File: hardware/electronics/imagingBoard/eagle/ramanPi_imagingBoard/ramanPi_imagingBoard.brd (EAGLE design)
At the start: 107.9 x 79.7 mm, 14 parts

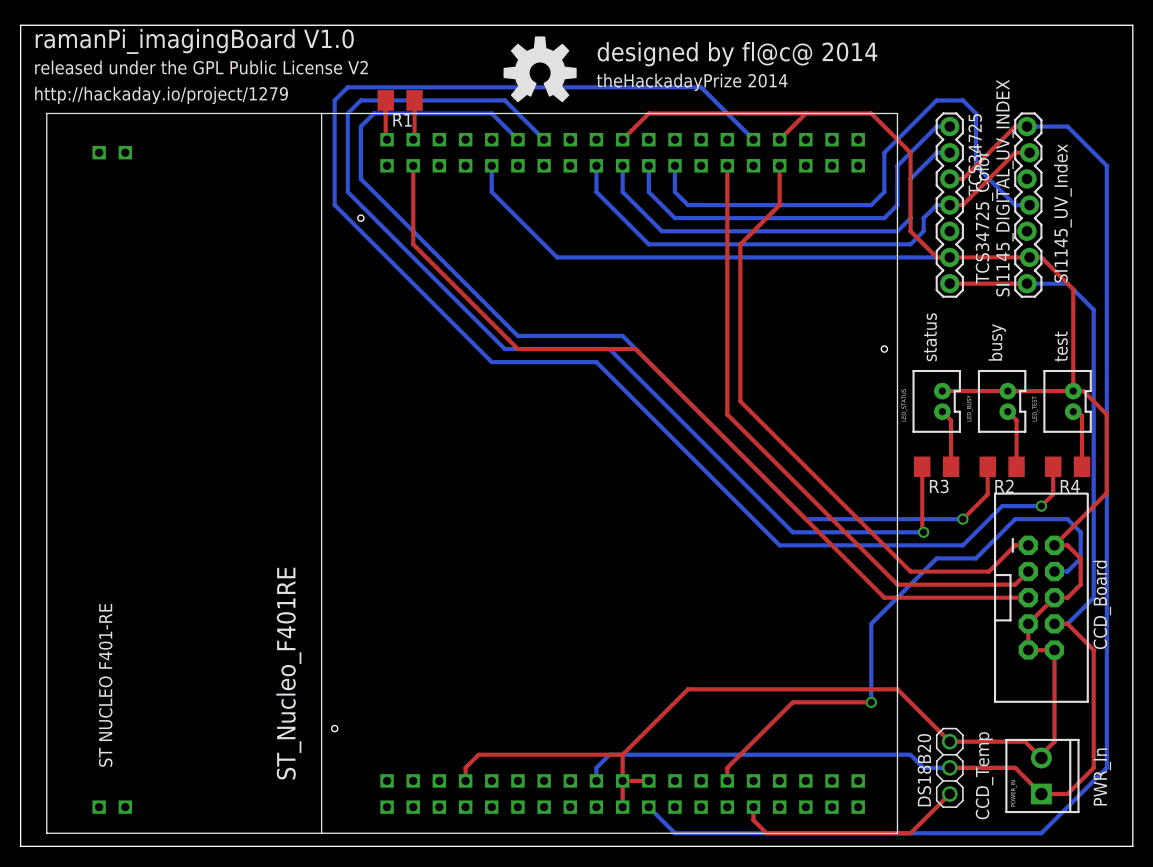
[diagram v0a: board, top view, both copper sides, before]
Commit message: imagingBoard updated
updated pin configuration for remote ccd board to match with new pinout
added ground plane and decoupling caps
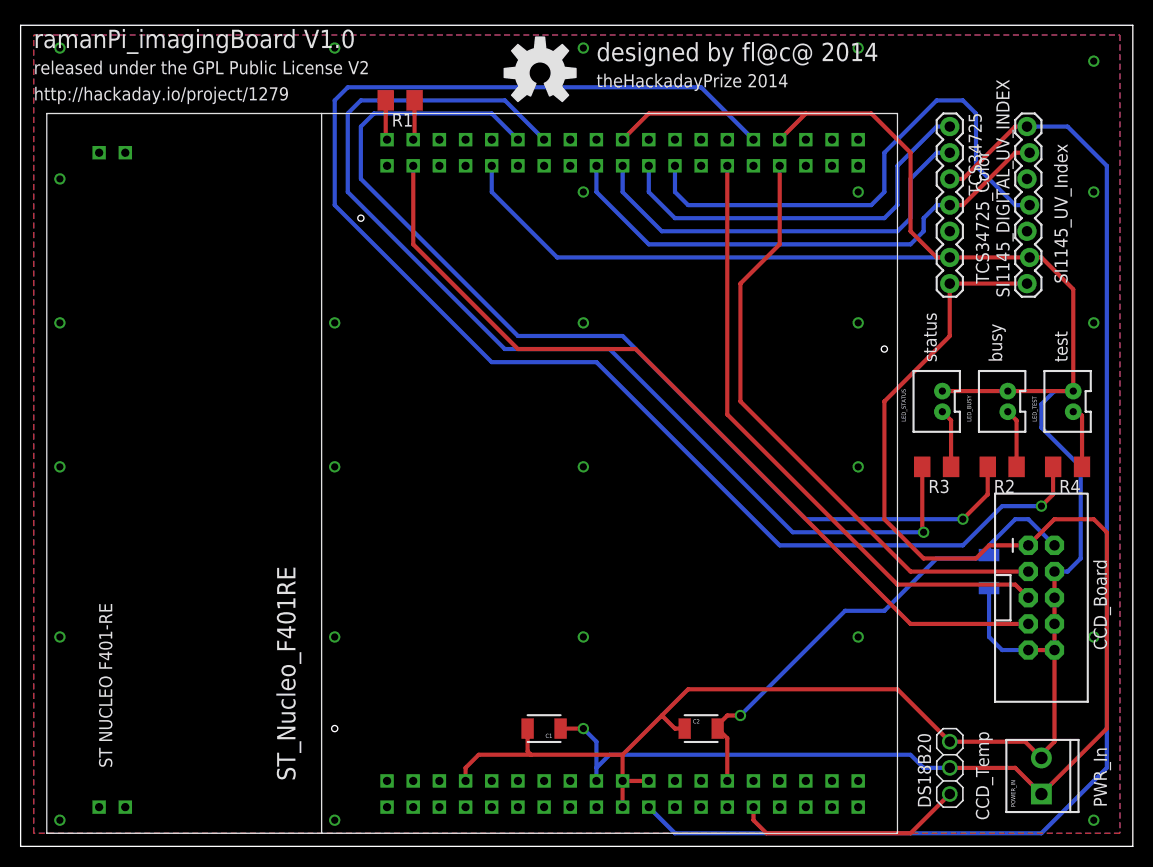
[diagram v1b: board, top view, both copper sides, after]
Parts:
- added C1, C2, C3: 0.1uf, SparkFun-Capacitors:1210
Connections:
- removed net N$3: CCD_BOARD.1, U$1.PB_3
- new net N$20: CCD_BOARD.3, U$1.PB_3
- net 5V: now also C1.1, CCD_BOARD.1; no longer CCD_BOARD.8
- net GND: now also C1.2, C2.1, C3.1, CCD_BOARD.4, CCD_BOARD.8; no longer CCD_BOARD.2, CCD_BOARD.7
- net N$1: now also CCD_BOARD.7; no longer CCD_BOARD.5
- net N$2: now also CCD_BOARD.5; no longer CCD_BOARD.3
- net N$9: now also C2.2, C3.2, CCD_BOARD.2; no longer CCD_BOARD.4
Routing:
- net N$3: track 60.3 -> 0.00 mm
- net N$20: track 0.00 -> 59.2 mm
- net 5V: track 116.8 -> 139.4 mm, vias 0 -> 1
- net GND: track 250.1 -> 261.7 mm, vias 0 -> 26
- net N$9: track 56.2 -> 48.4 mm
- net N$1: track 81.5 -> 82.6 mm
- added copper zone on layer 1, net GND
- added copper zone on layer 16, net GND

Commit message: updated Nucleo library in all board layouts
Updated Nucleo F401_RE library for better drill hole sizes
updated all boards to include new library changes
---need to update all studio files, svg, etc..
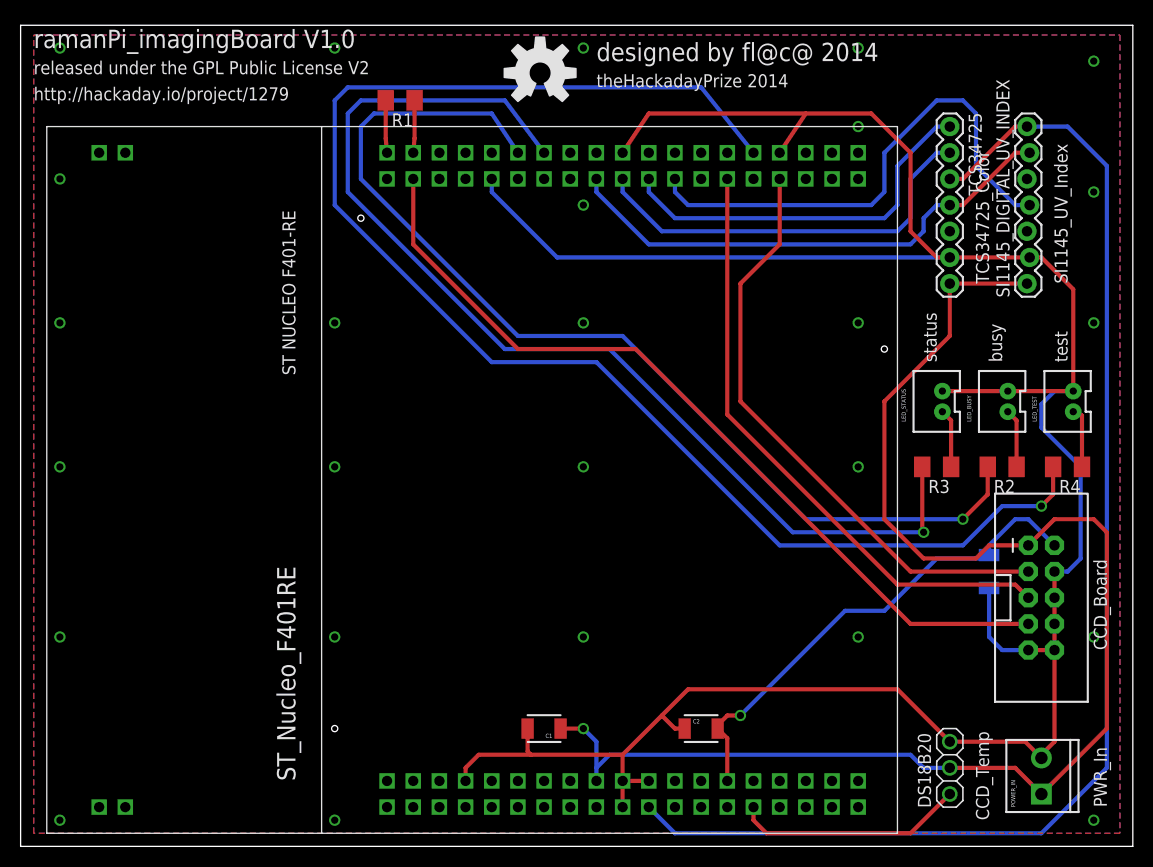
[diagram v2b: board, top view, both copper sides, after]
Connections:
- removed net NC6: U$1.NC6
- new net +3V3: U$1.+3V3
- new net U5V: U$1.U5V
- new net VIN: U$1.VIN
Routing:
- net N$8: track 51.1 -> 49.8 mm
- net N$20: track 59.2 -> 57.9 mm
- net N$2: track 60.7 -> 59.4 mm
- net N$12: track 38.7 -> 37.4 mm
- net N$11: track 41.3 -> 40.0 mm
- net N$10: track 51.1 -> 49.8 mm
- net N$1: track 82.6 -> 81.3 mm
- net N$5: track 3.86 -> 5.09 mm
- net N$4: track 3.86 -> 5.09 mm
- net N$16: track 100.1 -> 101.1 mm
- net N$17: track 104.9 -> 105.8 mm
- net N$18: track 141.5 -> 142.5 mm
- net GND: track 261.7 -> 262.4 mm
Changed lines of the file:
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@@
 </signal>
 <signal name="NC6">
-<contactref element="U$1" pad="NC6"/>
 </signal>
 <signal name="E5V">
@@
 <wire x1="59.69" y1="48.26" x2="48.26" y2="48.26" width="0.4064" layer="1"/>
 <wire x1="48.26" y1="48.26" x2="38.1" y2="58.42" width="0.4064" layer="1"/>
-<wire x1="38.1" y1="58.42" x2="38.1" y2="66.04" width="0.4064" layer="1"/>
+<wire x1="38.1" y1="58.42" x2="38.1" y2="64.77" width="0.4064" layer="1"/>
 <contactref element="CCD_BOARD" pad="7"/>
 <wire x1="86.36" y1="21.59" x2="97.79" y2="21.59" width="0.4064" layer="1"/>
@@
 <wire x1="96.52" y1="25.4" x2="85.09" y2="25.4" width="0.4064" layer="1"/>
 <wire x1="85.09" y1="25.4" x2="68.58" y2="41.91" width="0.4064" layer="1"/>
-<wire x1="68.58" y1="41.91" x2="68.58" y2="66.04" width="0.4064" layer="1"/>
+<wire x1="68.58" y1="41.91" x2="68.58" y2="64.77" width="0.4064" layer="1"/>
 <contactref element="CCD_BOARD" pad="5"/>
 <wire x1="96.52" y1="25.4" x2="97.79" y2="24.13" width="0.4064" layer="1"/>
@@
 <wire x1="86.36" y1="58.42" x2="60.96" y2="58.42" width="0.4064" layer="16"/>
 <wire x1="60.96" y1="58.42" x2="55.88" y2="63.5" width="0.4064" layer="16"/>
-<wire x1="55.88" y1="63.5" x2="55.88" y2="66.04" width="0.4064" layer="16"/>
+<wire x1="55.88" y1="63.5" x2="55.88" y2="64.77" width="0.4064" layer="16"/>
 <wire x1="90.17" y1="62.23" x2="91.44" y2="62.23" width="0.4064" layer="1"/>
 <wire x1="91.44" y1="62.23" x2="96.52" y2="67.31" width="0.4064" layer="1"/>
@@
 <wire x1="90.17" y1="57.15" x2="52.07" y2="57.15" width="0.4064" layer="16"/>
 <wire x1="52.07" y1="57.15" x2="45.72" y2="63.5" width="0.4064" layer="16"/>
-<wire x1="45.72" y1="63.5" x2="45.72" y2="66.04" width="0.4064" layer="16"/>
-<wire x1="73.66" y1="68.58" x2="76.2" y2="71.12" width="0.4064" layer="1"/>
+<wire x1="45.72" y1="63.5" x2="45.72" y2="64.77" width="0.4064" layer="16"/>
+<wire x1="73.66" y1="67.31" x2="76.2" y2="71.12" width="0.4064" layer="1"/>
 <wire x1="76.2" y1="71.12" x2="82.55" y2="71.12" width="0.4064" layer="1"/>
 <wire x1="82.55" y1="71.12" x2="86.36" y2="67.31" width="0.4064" layer="1"/>
@@
 <wire x1="86.36" y1="59.69" x2="88.9" y2="57.15" width="0.4064" layer="1"/>
 <wire x1="88.9" y1="57.15" x2="90.17" y2="57.15" width="0.4064" layer="1"/>
-<wire x1="58.42" y1="68.58" x2="60.96" y2="71.12" width="0.4064" layer="1"/>
+<wire x1="58.42" y1="67.31" x2="60.96" y2="71.12" width="0.4064" layer="1"/>
 <wire x1="60.96" y1="71.12" x2="76.2" y2="71.12" width="0.4064" layer="1"/>
 <contactref element="CCD_BOARD" pad="9"/>
@@
 <via x="81.28" y="77.47" extent="1-16" drill="0.7"/>
 <via x="3.81" y="64.77" extent="1-16" drill="0.7"/>
-<via x="54.61" y="63.5" extent="1-16" drill="0.7"/>
-<via x="81.28" y="63.5" extent="1-16" drill="0.7"/>
+<via x="54.61" y="62.23" extent="1-16" drill="0.7"/>
+<via x="81.28" y="69.85" extent="1-16" drill="0.7"/>
 <via x="104.14" y="63.5" extent="1-16" drill="0.7"/>
 <via x="104.14" y="50.8" extent="1-16" drill="0.7"/>
@@
 <contactref element="U$1" pad="PC_8-PWM3/3"/>
 <contactref element="R1" pad="2"/>
-<wire x1="35.56" y1="68.58" x2="35.43" y2="68.71" width="0.4064" layer="1"/>
+<wire x1="35.56" y1="67.31" x2="35.43" y2="68.71" width="0.4064" layer="1"/>
 <wire x1="35.43" y1="68.71" x2="35.43" y2="72.39" width="0.4064" layer="1"/>
 </signal>
@@
 <contactref element="U$1" pad="PC_6-PWM3/1"/>
 <contactref element="R1" pad="1"/>
-<wire x1="38.1" y1="68.58" x2="38.23" y2="68.71" width="0.4064" layer="1"/>
+<wire x1="38.1" y1="67.31" x2="38.23" y2="68.71" width="0.4064" layer="1"/>
 <wire x1="38.23" y1="68.71" x2="38.23" y2="72.39" width="0.4064" layer="1"/>
 </signal>
@@
 <wire x1="85.09" y1="59.69" x2="62.23" y2="59.69" width="0.4064" layer="16"/>
 <wire x1="62.23" y1="59.69" x2="58.42" y2="63.5" width="0.4064" layer="16"/>
-<wire x1="58.42" y1="63.5" x2="58.42" y2="66.04" width="0.4064" layer="16"/>
+<wire x1="58.42" y1="63.5" x2="58.42" y2="64.77" width="0.4064" layer="16"/>
 </signal>
 <signal name="N$12">
@@
 <wire x1="83.82" y1="60.96" x2="63.5" y2="60.96" width="0.4064" layer="16"/>
 <wire x1="63.5" y1="60.96" x2="60.96" y2="63.5" width="0.4064" layer="16"/>
-<wire x1="60.96" y1="63.5" x2="60.96" y2="66.04" width="0.4064" layer="16"/>
+<wire x1="60.96" y1="63.5" x2="60.96" y2="64.77" width="0.4064" layer="16"/>
 </signal>
 <signal name="N$10">
@@
 <wire x1="82.55" y1="62.23" x2="64.77" y2="62.23" width="0.4064" layer="16"/>
 <wire x1="64.77" y1="62.23" x2="63.5" y2="63.5" width="0.4064" layer="16"/>
-<wire x1="63.5" y1="63.5" x2="63.5" y2="66.04" width="0.4064" layer="16"/>
+<wire x1="63.5" y1="63.5" x2="63.5" y2="64.77" width="0.4064" layer="16"/>
 </signal>
 <signal name="N$13">
@@
 <contactref element="U$1" pad="PA_12"/>
 <contactref element="R2" pad="2"/>
-<wire x1="48.26" y1="68.58" x2="45.72" y2="71.12" width="0.4064" layer="16"/>
+<wire x1="48.26" y1="67.31" x2="45.72" y2="71.12" width="0.4064" layer="16"/>
 <wire x1="45.72" y1="71.12" x2="34.29" y2="71.12" width="0.4064" layer="16"/>
 <wire x1="34.29" y1="71.12" x2="33.02" y2="69.85" width="0.4064" layer="16"/>
@@
 <contactref element="R3" pad="2"/>
 <wire x1="87.5" y1="36.83" x2="87.63" y2="36.83" width="0.4064" layer="1"/>
-<wire x1="50.8" y1="68.58" x2="46.99" y2="72.39" width="0.4064" layer="16"/>
+<wire x1="50.8" y1="67.31" x2="46.99" y2="72.39" width="0.4064" layer="16"/>
 <wire x1="46.99" y1="72.39" x2="33.02" y2="72.39" width="0.4064" layer="16"/>
 <wire x1="33.02" y1="72.39" x2="31.75" y2="71.12" width="0.4064" layer="16"/>
@@
 <contactref element="U$1" pad="PB_13-PWM1/1N-SCK"/>
 <contactref element="R4" pad="2"/>
-<wire x1="71.12" y1="68.58" x2="66.04" y2="73.66" width="0.4064" layer="16"/>
+<wire x1="71.12" y1="67.31" x2="66.04" y2="73.66" width="0.4064" layer="16"/>
 <wire x1="66.04" y1="73.66" x2="31.75" y2="73.66" width="0.4064" layer="16"/>
 <wire x1="31.75" y1="73.66" x2="30.48" y2="72.39" width="0.4064" layer="16"/>
@@
 <wire x1="69.85" y1="43.18" x2="69.85" y2="54.61" width="0.4064" layer="1"/>
 <wire x1="69.85" y1="54.61" x2="73.66" y2="58.42" width="0.4064" layer="1"/>
-<wire x1="73.66" y1="58.42" x2="73.66" y2="66.04" width="0.4064" layer="1"/>
+<wire x1="73.66" y1="58.42" x2="73.66" y2="64.77" width="0.4064" layer="1"/>
+</signal>
+<signal name="U5V">
+<contactref element="U$1" pad="U5V"/>
+</signal>
+<signal name="+3V3">
+<contactref element="U$1" pad="+3V3"/>
+</signal>
+<signal name="VIN">
+<contactref element="U$1" pad="VIN"/>
 </signal>
 </signals>

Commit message: update
updated all boards and schematics
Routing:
- net GND: track 262.4 -> 261.6 mm
- net N$7: track 125.5 -> 126.2 mm
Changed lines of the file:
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@@
 <contactref element="SI1145_DIGITAL_UV_INDEX" pad="7"/>
 <contactref element="TCS34725" pad="3"/>
-<wire x1="60.96" y1="3.81" x2="63.5" y2="1.27" width="0.4064" layer="16"/>
-<wire x1="63.5" y1="1.27" x2="99.06" y2="1.27" width="0.4064" layer="16"/>
+<wire x1="62.23" y1="1.27" x2="99.06" y2="1.27" width="0.4064" layer="16"/>
 <wire x1="99.06" y1="1.27" x2="105.41" y2="7.62" width="0.4064" layer="16"/>
 <wire x1="105.41" y1="7.62" x2="105.41" y2="66.04" width="0.4064" layer="16"/>
@@
 <wire x1="91.44" y1="64.77" x2="96.52" y2="69.85" width="0.4064" layer="1"/>
 <wire x1="96.52" y1="69.85" x2="97.663" y2="69.85" width="0.4064" layer="1"/>
+<wire x1="62.23" y1="1.27" x2="60.96" y2="2.54" width="0.4064" layer="16"/>
+<wire x1="60.96" y1="2.54" x2="60.96" y2="3.81" width="0.4064" layer="16"/>
 </signal>
 <signal name="N$8">
@@
 <wire x1="52.07" y1="57.15" x2="45.72" y2="63.5" width="0.4064" layer="16"/>
 <wire x1="45.72" y1="63.5" x2="45.72" y2="64.77" width="0.4064" layer="16"/>
-<wire x1="73.66" y1="67.31" x2="76.2" y2="71.12" width="0.4064" layer="1"/>
-<wire x1="76.2" y1="71.12" x2="82.55" y2="71.12" width="0.4064" layer="1"/>
 <wire x1="82.55" y1="71.12" x2="86.36" y2="67.31" width="0.4064" layer="1"/>
 <wire x1="86.36" y1="67.31" x2="86.36" y2="59.69" width="0.4064" layer="1"/>
@@
 <wire x1="88.9" y1="57.15" x2="90.17" y2="57.15" width="0.4064" layer="1"/>
 <wire x1="58.42" y1="67.31" x2="60.96" y2="71.12" width="0.4064" layer="1"/>
-<wire x1="60.96" y1="71.12" x2="76.2" y2="71.12" width="0.4064" layer="1"/>
+<wire x1="60.96" y1="71.12" x2="73.66" y2="71.12" width="0.4064" layer="1"/>
 <contactref element="CCD_BOARD" pad="9"/>
 <contactref element="CCD_BOARD" pad="4"/>
@@
 <contactref element="C2" pad="1"/>
 <contactref element="C3" pad="1"/>
+<wire x1="73.66" y1="71.12" x2="82.55" y2="71.12" width="0.4064" layer="1"/>
 <wire x1="100.33" y1="10.16" x2="100.33" y2="19.05" width="0.4064" layer="1"/>
 <wire x1="64.44" y1="11.43" x2="63.5" y2="11.43" width="0.4064" layer="1"/>
@@
 <vertex x="1.27" y="1.27"/>
 </polygon>
+<wire x1="73.66" y1="67.31" x2="73.66" y2="71.12" width="0.4064" layer="1"/>
 </signal>
 <signal name="5V">
@@
 <contactref element="U$1" pad="PB_13-PWM1/1N-SCK"/>
 <contactref element="R4" pad="2"/>
-<wire x1="71.12" y1="67.31" x2="66.04" y2="73.66" width="0.4064" layer="16"/>
 <wire x1="66.04" y1="73.66" x2="31.75" y2="73.66" width="0.4064" layer="16"/>
 <wire x1="31.75" y1="73.66" x2="30.48" y2="72.39" width="0.4064" layer="16"/>
@@
 <wire x1="99.06" y1="33.02" x2="100.2" y2="34.16" width="0.4064" layer="1"/>
 <wire x1="100.2" y1="34.16" x2="100.2" y2="36.83" width="0.4064" layer="1"/>
+<wire x1="66.04" y1="73.66" x2="71.12" y2="68.58" width="0.4064" layer="16"/>
+<wire x1="71.12" y1="68.58" x2="71.12" y2="67.31" width="0.4064" layer="16"/>
 </signal>
 <signal name="N$20">
@@
 </signal>
 </signals>
-<errors>
-</errors>
 </board>
 </drawing>

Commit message: added reset circuitry to all stm32 boards
added reset circuitry for raspi to reset each board from remote.
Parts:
- added Q1: 2n2222, semicon-smd-ipc:SOT23
- added R5: 10k, adafruit:M1206
- added RASPI_RESET: M02JST-PTH-VERT, SparkFun-Connectors:JST-2-PTH-VERT
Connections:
- new net N$19: Q1.3, R5.1, U$1.NRST
- new net N$3: Q1.1, RASPI_RESET.1
- net 5V: now also R5.2
- net GND: now also Q1.2, RASPI_RESET.2
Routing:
- net N$3: track 0.00 -> 44.0 mm
- net N$19: track 0.00 -> 16.4 mm, vias 0 -> 1
- net 5V: track 139.4 -> 143.3 mm
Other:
- board text added: "raspiReset"
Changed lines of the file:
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@@
 <text x="95.25" y="46.99" size="1.27" layer="21" font="vector" rot="R90">busy</text>
 <text x="101.6" y="46.99" size="1.27" layer="21" font="vector" rot="R90">test</text>
+<text x="87.63" y="13.97" size="1.778" layer="21" rot="R90">raspiReset</text>
 </plain>
 <attributes>
@@
 </classes>
 <designrules>
-<description language="de">&lt;b&gt;EAGLE Design Rules&lt;/b&gt;
-&lt;p&gt;
-Die Standard-Design-Rules sind so gewählt, dass sie für
-die meisten Anwendungen passen. Sollte ihre Platine
-besondere Anforderungen haben, treffen Sie die erforderlichen
-Einstellungen hier und speichern die Design Rules unter
-einem neuen Namen ab.</description>
 <description language="en">&lt;b&gt;EAGLE Design Rules&lt;/b&gt;
 &lt;p&gt;
@@
 <param name="mdViaViaSameLayer" value="8mil"/>
 <param name="mnLayersViaInSmd" value="2"/>
-<param name="mdCopperDimension" value="40mil"/>
+<param name="mdCopperDimension" value="10mil"/>
 <param name="mdDrill" value="8mil"/>
 <param name="mdSmdStop" value="0mil"/>
-<param name="msWidth" value="10mil"/>
-<param name="msDrill" value="24mil"/>
+<param name="msWidth" value="8mil"/>
+<param name="msDrill" value="20mil"/>
 <param name="msMicroVia" value="9.99mm"/>
 <param name="msBlindViaRatio" value="0.5"/>
@@
 <param name="rvMicroViaOuter" value="0.25"/>
 <param name="rvMicroViaInner" value="0.25"/>
-<param name="rlMinPadTop" value="10mil"/>
+<param name="rlMinPadTop" value="12mil"/>
 <param name="rlMaxPadTop" value="20mil"/>
 <param name="rlMinPadInner" value="10mil"/>
 <param name="rlMaxPadInner" value="20mil"/>
-<param name="rlMinPadBottom" value="10mil"/>
+<param name="rlMinPadBottom" value="12mil"/>
 <param name="rlMaxPadBottom" value="20mil"/>
-<param name="rlMinViaOuter" value="8mil"/>
+<param name="rlMinViaOuter" value="10mil"/>
 <param name="rlMaxViaOuter" value="20mil"/>
-<param name="rlMinViaInner" value="8mil"/>
+<param name="rlMinViaInner" value="10mil"/>
 <param name="rlMaxViaInner" value="20mil"/>
 <param name="rlMinMicroViaOuter" value="4mil"/>
@@
 <param name="mlMinCreamFrame" value="0mil"/>
 <param name="mlMaxCreamFrame" value="0mil"/>
-<param name="mlViaStopLimit" value="0mil"/>
+<param name="mlViaStopLimit" value="25mil"/>
 <param name="srRoundness" value="0"/>
 <param name="srMinRoundness" value="0mil"/>
@@
 <element name="C2" library="SparkFun-Capacitors" package="1210" value="0.1uf" x="66.04" y="11.43"/>
 <element name="C3" library="SparkFun-Capacitors" package="1210" value="0.1uf" x="93.98" y="26.67" rot="MR90"/>
+<element name="Q1" library="semicon-smd-ipc" package="SOT23" value="2n2222" x="45.72" y="17.78" rot="R180"/>
+<element name="R5" library="adafruit" package="M1206" value="10k" x="50.8" y="15.24"/>
+<element name="RASPI_RESET" library="SparkFun-Connectors" package="JST-2-PTH-VERT" value="M02JST-PTH-VERT" x="90.17" y="17.78" rot="R270"/>
 </elements>
 <signals>
@@
 </polygon>
 <wire x1="73.66" y1="67.31" x2="73.66" y2="71.12" width="0.4064" layer="1"/>
+<contactref element="Q1" pad="2"/>
+<contactref element="RASPI_RESET" pad="2"/>
 </signal>
 <signal name="5V">
@@
 <wire x1="83.82" y1="43.18" x2="90.17" y2="49.53" width="0.4064" layer="1"/>
 <wire x1="90.17" y1="49.53" x2="90.17" y2="54.61" width="0.4064" layer="1"/>
+<contactref element="R5" pad="2"/>
+<wire x1="52.4" y1="11.43" x2="52.4" y2="15.04" width="0.4064" layer="1"/>
+<wire x1="52.4" y1="15.04" x2="52.2" y2="15.24" width="0.4064" layer="1"/>
 </signal>
 <signal name="N$4">
@@
 <contactref element="U$1" pad="VIN"/>
 </signal>
+<signal name="N$19">
+<contactref element="U$1" pad="NRST"/>
+<contactref element="Q1" pad="3"/>
+<contactref element="R5" pad="1"/>
+<wire x1="49.4" y1="15.24" x2="47.16" y2="15.24" width="0.4064" layer="1"/>
+<wire x1="47.16" y1="15.24" x2="45.72" y2="16.68" width="0.4064" layer="1"/>
+<wire x1="49.4" y1="15.24" x2="48.26" y2="15.24" width="0.4064" layer="1"/>
+<wire x1="48.26" y1="15.24" x2="46.99" y2="13.97" width="0.4064" layer="1"/>
+<wire x1="46.99" y1="13.97" x2="46.99" y2="11.43" width="0.4064" layer="1"/>
+<via x="46.99" y="11.43" extent="1-16" drill="0.7"/>
+<wire x1="50.8" y1="6.35" x2="50.8" y2="7.62" width="0.4064" layer="16"/>
+<wire x1="50.8" y1="7.62" x2="46.99" y2="11.43" width="0.4064" layer="16"/>
+</signal>
+<signal name="N$3">
+<contactref element="RASPI_RESET" pad="1"/>
+<contactref element="Q1" pad="1"/>
+<wire x1="89.62" y1="18.78" x2="87.36" y2="18.78" width="0.4064" layer="1"/>
+<wire x1="87.36" y1="18.78" x2="86.36" y2="17.78" width="0.4064" layer="1"/>
+<wire x1="86.36" y1="17.78" x2="49.53" y2="17.78" width="0.4064" layer="1"/>
+<wire x1="49.53" y1="17.78" x2="48.26" y2="19.05" width="0.4064" layer="1"/>
+<wire x1="48.26" y1="19.05" x2="46.84" y2="19.05" width="0.4064" layer="1"/>
+<wire x1="46.84" y1="19.05" x2="46.67" y2="18.88" width="0.4064" layer="1"/>
+</signal>
 </signals>
